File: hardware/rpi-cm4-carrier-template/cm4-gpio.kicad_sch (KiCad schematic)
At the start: 1 part

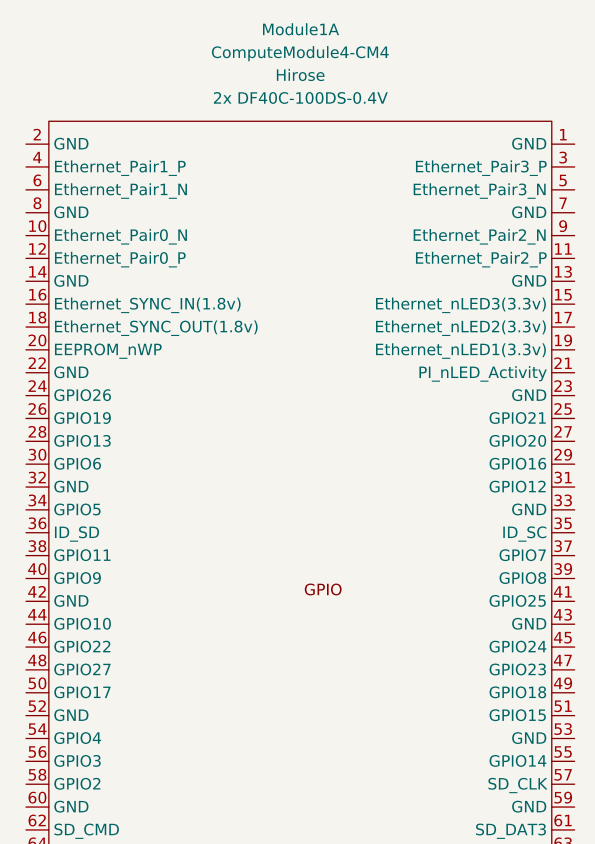
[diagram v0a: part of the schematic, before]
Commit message: Added dimensions and updated CM4 component properties to include both receptacle options
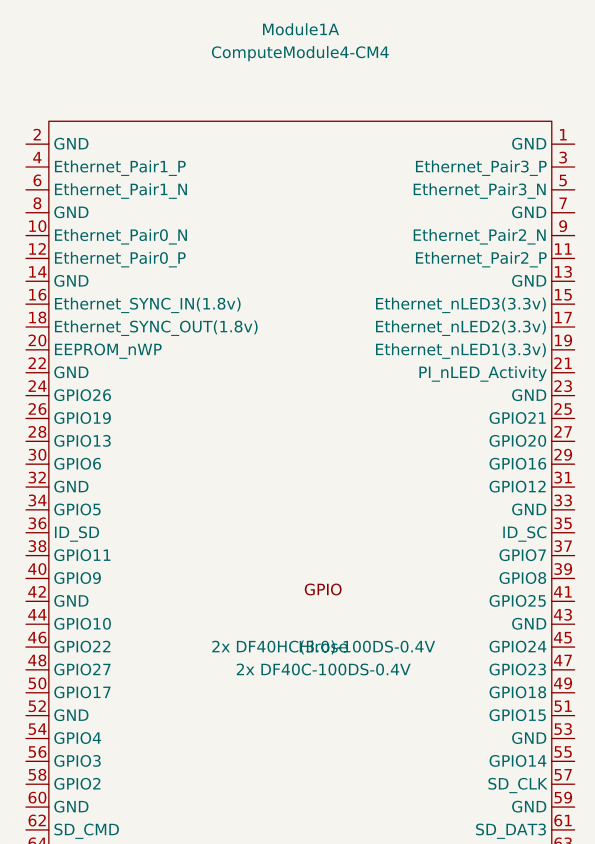
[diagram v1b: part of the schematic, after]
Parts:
- Module1: Field4 Hirose -> (none); Field5 2x DF40C-100DS-0.4V -> (none); MPN (none) -> 2x DF40C-100DS-0.4V; MPN (Alt) (none) -> 2x DF40HC(3.0)-100DS-0.4V; Manufacturer (none) -> Hirose
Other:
- title: Raspberry Pi Compute Module 4 Shoe Template -> Raspberry Pi Compute Module 4 Carrier Template
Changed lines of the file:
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@@
   (paper "A4")
   (title_block
-    (title "Raspberry Pi Compute Module 4 Shoe Template")
+    (title "Raspberry Pi Compute Module 4 Carrier Template")
     (date "2020-10-31")
     (rev "v01")
@@
       (effects (font (size 1.27 1.27)) hide)
     )
-    (property "Field4" "Hirose" (id 4) (at 73.66 38.1 0))
-    (property "Field5" "2x DF40C-100DS-0.4V" (id 5) (at 73.66 40.64 0))
+    (property "Manufacturer" "Hirose" (id 8) (at 76.2 101.6 0))
+    (property "MPN" "2x DF40C-100DS-0.4V" (id 9) (at 76.2 104.14 0))
+    (property "MPN (Alt)" "2x DF40HC(3.0)-100DS-0.4V" (id 10) (at 76.2 101.6 0))
     (property "Digi-Key_PN" "2x H11615CT-ND" (id 6) (at 76.2 101.6 0)
       (effects (font (size 1.27 1.27)) hide)

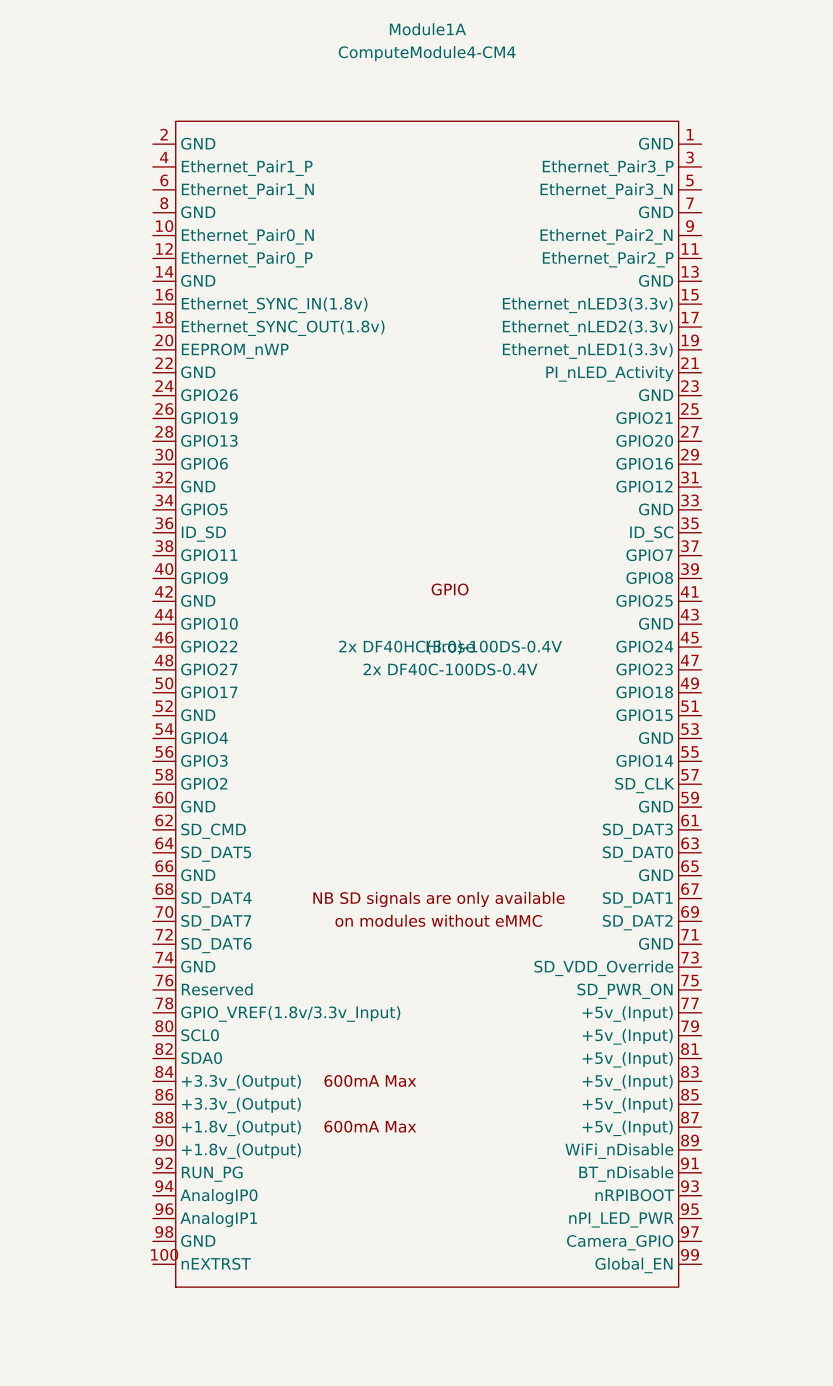
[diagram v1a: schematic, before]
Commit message: Added GND and power lines with labels
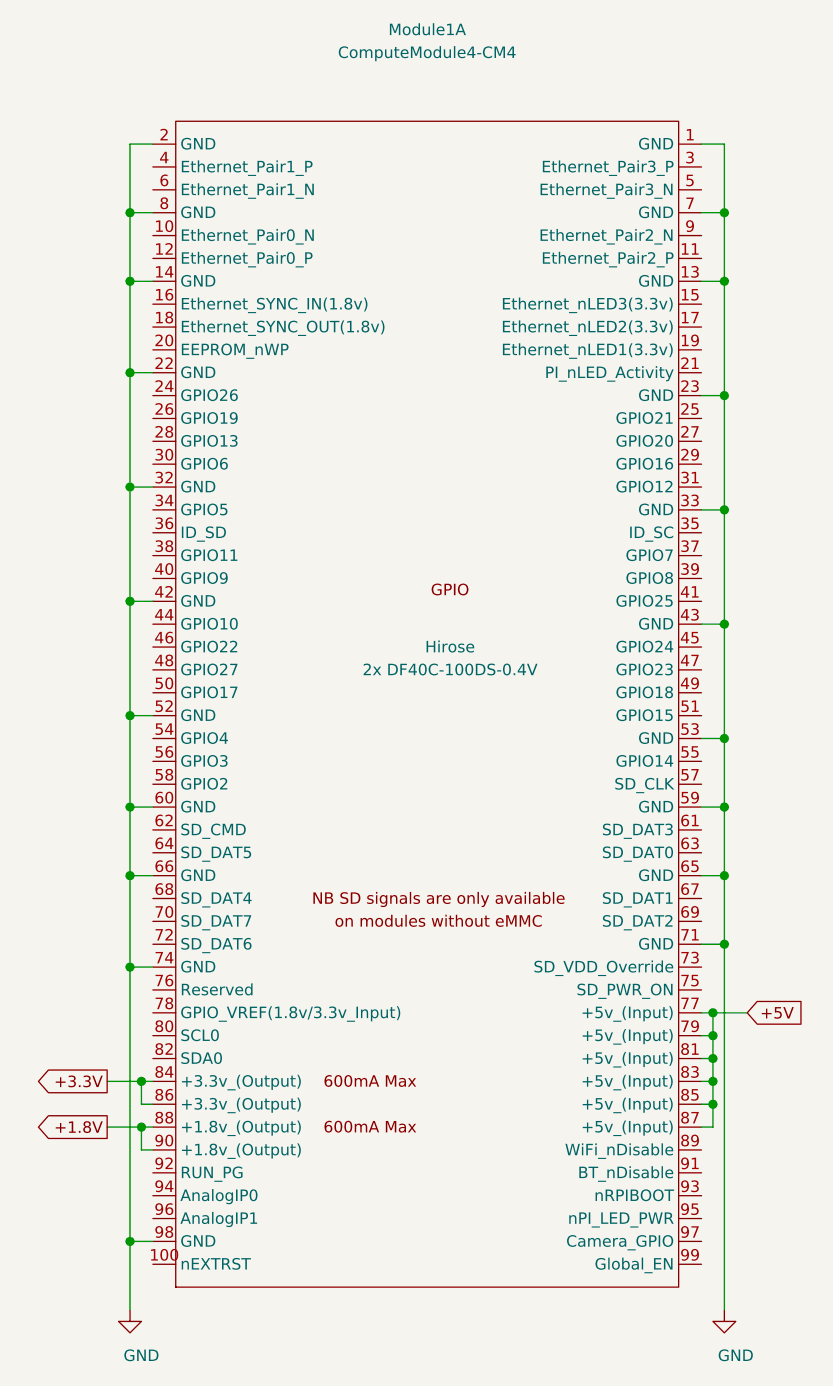
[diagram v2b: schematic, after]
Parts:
- Module1: MPN (Alt) 2x DF40HC(3.0)-100DS-0.4V -> (none)
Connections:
- net GND: now reaches Module1.1 (GND)
- net GND: now also Module1.13 (GND), Module1.14 (GND), Module1.2 (GND), Module1.22 (GND), Module1.23 (GND), Module1.32 (GND), Module1.33 (GND), Module1.42 (GND), Module1.43 (GND), Module1.52 (GND), Module1.53 (GND), Module1.59 (GND), Module1.60 (GND), Module1.65 (GND), Module1.66 (GND), Module1.7 (GND), Module1.71 (GND), Module1.74 (GND), Module1.8 (GND), Module1.98 (GND)
- net +5V: now reaches Module1.77 (+5v_(Input))
- net +5V: now also Module1.79 (+5v_(Input)), Module1.81 (+5v_(Input)), Module1.83 (+5v_(Input)), Module1.85 (+5v_(Input)), Module1.87 (+5v_(Input))
- net +3.3V: now reaches Module1.84 (+3.3v_(Output))
- net +3.3V: now also Module1.86 (+3.3v_(Output))
- net +1.8V: now reaches Module1.88 (+1.8v_(Output))
- net +1.8V: now also Module1.90 (+1.8v_(Output))
